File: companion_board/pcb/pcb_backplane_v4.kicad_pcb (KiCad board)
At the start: 4 copper layers, 120 x 100 mm, 8 parts

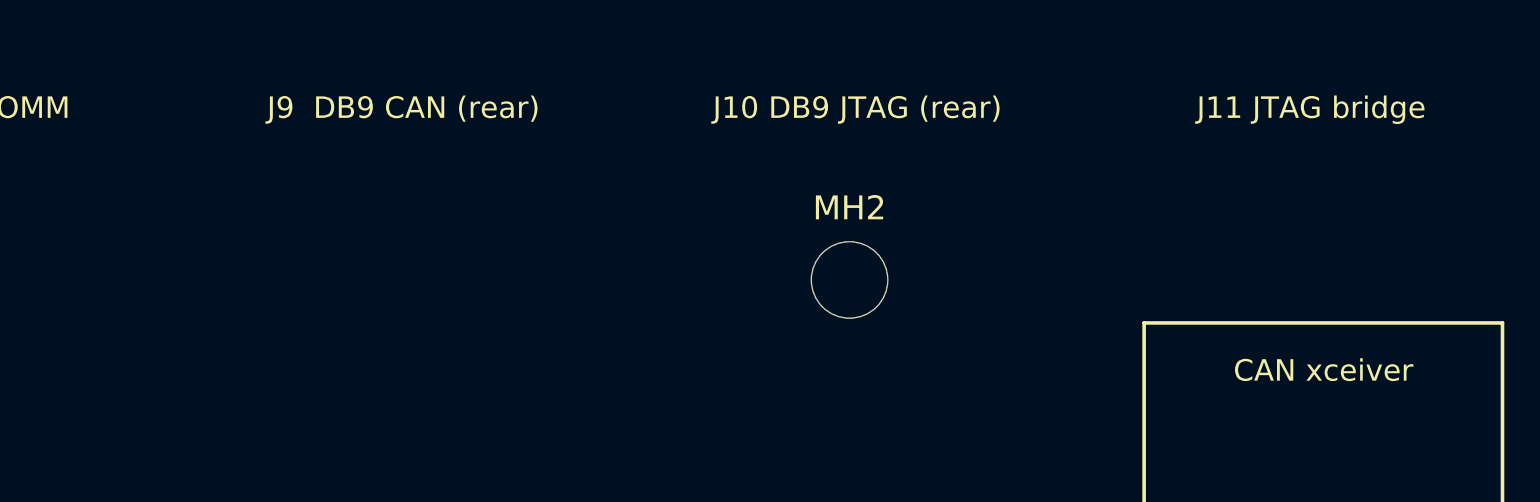
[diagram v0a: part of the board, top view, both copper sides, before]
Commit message: companion_board: v4.1 NC-pin policy (GND fill + R3 nTRST pull-up)
Tie spare pins on the rear DB9 connectors to the backplane GND rail
where electrically safe, formalised as a new "NC-pin policy" in
PCB_BACKPLANE_PINOUT.md §1.7. Also reaffirm in a new §1.6 what the
backplane intentionally does NOT route (front DB25-3 -> host LPT,
front pushbuttons #2 and #3, SPI).

- DB9-CAN (J9) spare pins 1, 4, 6, 8, 9 -> GND for in-cable shielding.
  Deviates from CiA 303-1 reservation of pins 1/9 for optional CAN_V+;
  documented caveat and silkscreen note next to J9 for users plugging
  into a CANopen network that sources V+.
- DB9-JTAG (J10) pin 7 (nTRST) -> NOT GND (would hold the JTAG TAP
  in permanent reset). New R3 = 10 kohm THT axial pulls nTRST HIGH
  to +3.3 V so the TAP is "not in reset" by default; a JTAG cable
  that needs TAP-RST can still drive it low through the pull-up.
- J11 JTAG bridge pin 7 (KEY position) -> GND, harmless and shields
  the adjacent TDI line on the pigtail.
- H_D22 pair 17/18 and other bottom-side mating-header NC pins stay
  NC; some Mega R3 / Due revisions route 5 V or GND there and a
  backplane-side ground would short.

Updated SVG top sketch, KiCad silkscreen guides, and pcb/README.md
placement table to include R3. Changelog entries added to both
PCB_BACKPLANE_PINOUT.md (v4.1) and DEVICE_PINOUT.md (1.4).
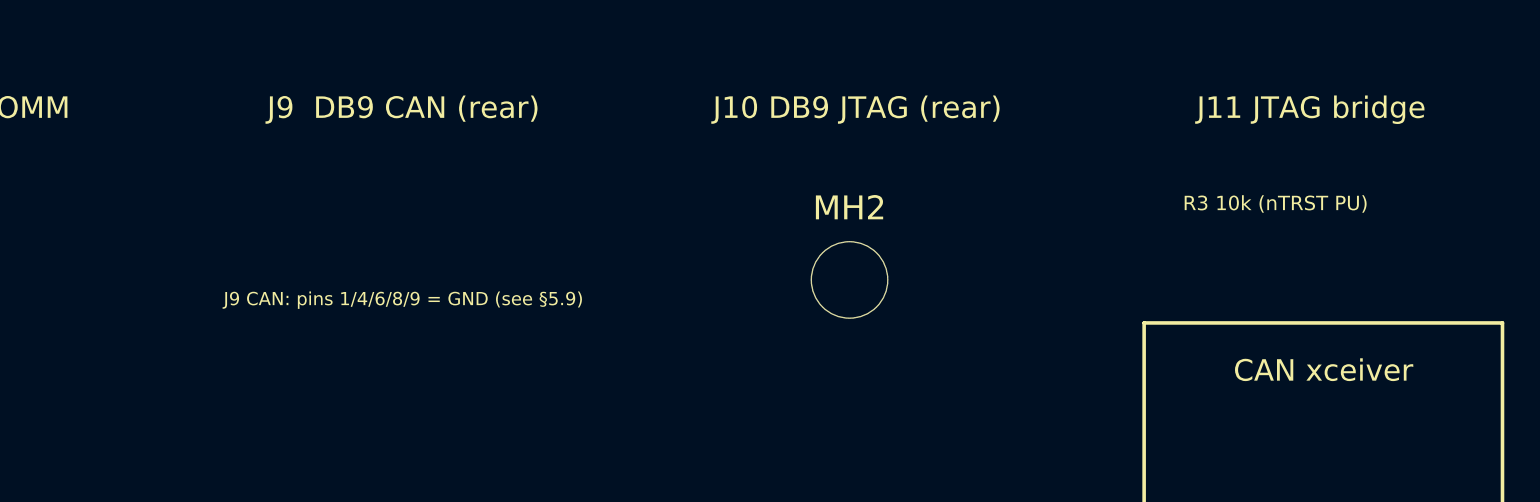
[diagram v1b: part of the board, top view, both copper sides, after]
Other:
- board text added: "J9 CAN: pins 1/4/6/8/9 = GND (see §5.9)"
- board text added: "R3 10k (nTRST PU)"
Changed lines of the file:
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@@
 		(effects (font (size 0.6 0.6) (thickness 0.10)))
+	)
+	;; R3 10k pull-up on DB9-JTAG pin 7 (nTRST). KiCad at (108, 49).
+	;; See PCB_BACKPLANE_PINOUT.md §5.10.
+	(gr_text "R3 10k (nTRST PU)" (at 108 46 0)
+		(layer "F.SilkS")
+		(effects (font (size 0.6 0.6) (thickness 0.10)))
+	)
+	;; Silk note next to J9 (DB9-CAN rear) for the deliberate
+	;; CiA 303-1 deviation (GND on spare pins).
+	(gr_text "J9 CAN: pins 1/4/6/8/9 = GND (see §5.9)" (at 71.5 50 0)
+		(layer "F.SilkS")
+		(effects (font (size 0.55 0.55) (thickness 0.10)))
 	)
 	;; Board ID silkscreen (top side, near MH3)
